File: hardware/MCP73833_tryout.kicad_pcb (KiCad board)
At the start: 2 copper layers, 55 x 30 mm, 14 parts, among them J1 LOAD, J2 BAT, U1 MCP73833, U2 USB_Micro

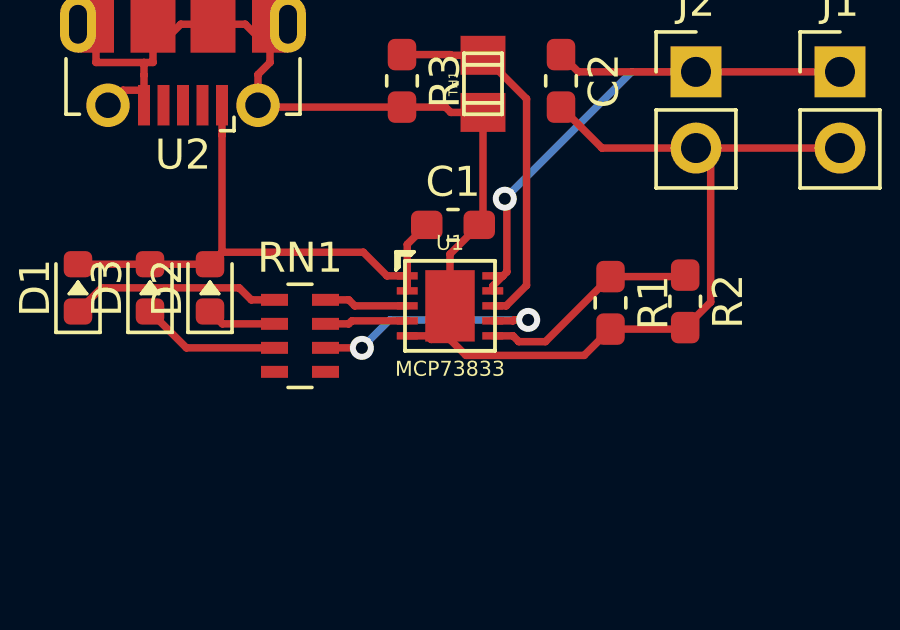
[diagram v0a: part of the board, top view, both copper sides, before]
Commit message: update for MCP73833 DFN,
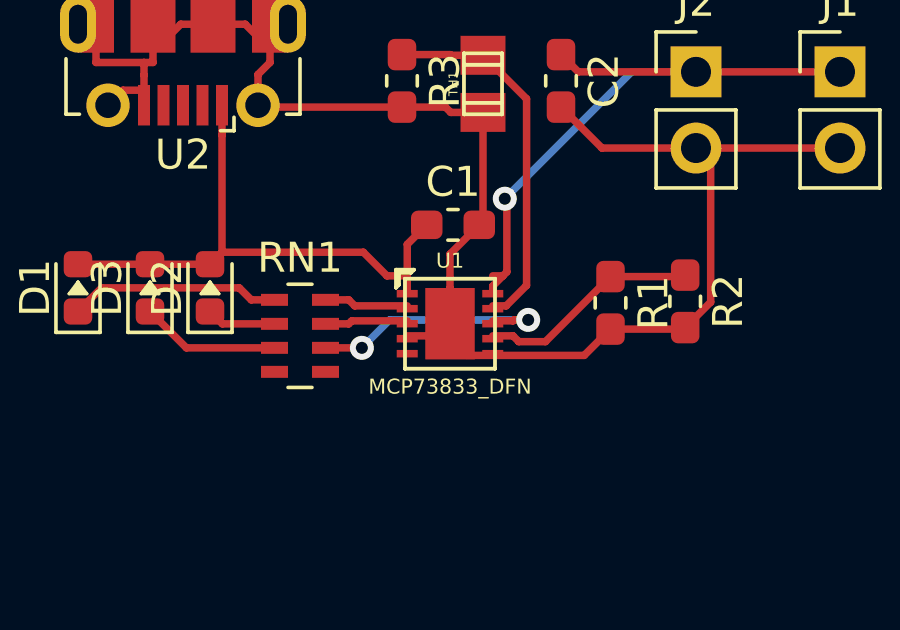
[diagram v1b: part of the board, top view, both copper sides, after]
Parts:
- U1: value MCP73833 -> MCP73833_DFN; footprint footprint-lib:MCP73833 -> footprint-lib:MCP73833_DFN
- moved U1 0.59 mm to (37.0, 31.6)
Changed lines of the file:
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@@
     (add_net "Net-(R1-Pad1)")
     (add_net "Net-(R3-Pad1)")
+    (add_net "Net-(RN1-Pad4)")
+    (add_net "Net-(RN1-Pad5)")
     (add_net "Net-(RN1-Pad6)")
     (add_net "Net-(RN1-Pad7)")
     (add_net "Net-(RN1-Pad8)")
+    (add_net "Net-(U2-Pad2)")
+    (add_net "Net-(U2-Pad3)")
+    (add_net "Net-(U2-Pad4)")
+  )
+  (module footprint-lib:MCP73833_DFN (layer F.Cu)
+    (at 37 31.595)
+    (descr "Plastic DFN, 10 pins, 3x3, Linear Technology")
+    (tags MCP73833_DFN)
+    (fp_text reference U1 (at 0 -2.1) (layer F.SilkS)
+      (effects (font (size 0.5 0.5) (thickness 0.1)))
+    )
+    (fp_text value MCP73833_DFN (at 0 2.1) (layer F.SilkS)
+      (effects (font (size 0.5 0.5) (thickness 0.1)))
+    )
+    (fp_line (start -1.7 -1.3) (end -1.8 -1.2) (layer F.SilkS) (width 0.127))
+    (fp_line (start -1.8 -1.2) (end -1.8 -1.8) (layer F.SilkS) (width 0.127))
+    (fp_line (start -1.8 -1.8) (end -1.2 -1.8) (layer F.SilkS) (width 0.127))
+    (fp_line (start -1.2 -1.8) (end -1.3 -1.7) (layer F.SilkS) (width 0.127))
+    (fp_line (start -1.3 -1.7) (end -1.7 -1.7) (layer F.SilkS) (width 0.127))
+    (fp_line (start -1.7 -1.7) (end -1.7 -1.3) (layer F.SilkS) (width 0.127))
+    (fp_line (start -1.5 -1.5) (end -1.5 1.5) (layer F.SilkS) (width 0.127))
+    (fp_line (start -1.5 1.5) (end 1.5 1.5) (layer F.SilkS) (width 0.127))
+    (fp_line (start 1.5 1.5) (end 1.5 -1.5) (layer F.SilkS) (width 0.127))
+    (fp_line (start 1.5 -1.5) (end -1.5 -1.5) (layer F.SilkS) (width 0.127))
+    (pad 1 smd rect (at -1.425 -1) (size 0.7 0.25) (layers F.Cu F.Paste F.Mask)
+      (net 2 +5V) (solder_mask_margin 0.07))
+    (pad 2 smd rect (at -1.425 -0.5) (size 0.7 0.25) (layers F.Cu F.Paste F.Mask)
+      (net 2 +5V) (solder_mask_margin 0.07))
+    (pad 3 smd rect (at -1.425 0) (size 0.7 0.25) (layers F.Cu F.Paste F.Mask)
+      (net 11 "Net-(RN1-Pad8)") (solder_mask_margin 0.07))
+    (pad 4 smd rect (at -1.425 0.5) (size 0.7 0.25) (layers F.Cu F.Paste F.Mask)
+      (net 10 "Net-(RN1-Pad7)") (solder_mask_margin 0.07))
+    (pad 5 smd rect (at -1.425 1) (size 0.7 0.25) (layers F.Cu F.Paste F.Mask)
+      (net 1 GND) (solder_mask_margin 0.07))
+    (pad 6 smd rect (at 1.425 1) (size 0.7 0.25) (layers F.Cu F.Paste F.Mask)
+      (net 7 "Net-(R1-Pad1)") (solder_mask_margin 0.07))
+    (pad 7 smd rect (at 1.425 0.5) (size 0.7 0.25) (layers F.Cu F.Paste F.Mask)
+      (net 9 "Net-(RN1-Pad6)") (solder_mask_margin 0.07))
+    (pad 8 smd rect (at 1.425 0) (size 0.7 0.25) (layers F.Cu F.Paste F.Mask)
+      (net 8 "Net-(R3-Pad1)") (solder_mask_margin 0.07))
+    (pad 9 smd rect (at 1.425 -0.5) (size 0.7 0.25) (layers F.Cu F.Paste F.Mask)
+      (net 3 "Net-(C2-Pad1)") (solder_mask_margin 0.07))
+    (pad 10 smd rect (at 1.425 -1) (size 0.7 0.25) (layers F.Cu F.Paste F.Mask)
+      (net 3 "Net-(C2-Pad1)") (solder_mask_margin 0.07))
+    (pad 11 smd rect (at 0 -0.595) (size 1.65 1.19) (layers F.Cu F.Paste F.Mask)
+      (net 1 GND) (solder_mask_margin 0.07) (solder_paste_margin -0.1))
+    (pad 11 smd rect (at 0 0.595) (size 1.65 1.19) (layers F.Cu F.Paste F.Mask)
+      (net 1 GND) (solder_mask_margin 0.07) (solder_paste_margin -0.1))
+    (model ${HOME}/_workspace/kicad/kicad_library/smisioto-footprints/modules/packages3d/walter/smd_qfn/dfn10_3x3.wrl
+      (at (xyz 0 0 0))
+      (scale (xyz 1 1 1))
+      (rotate (xyz 0 0 0))
+    )
   )
   (module footprint-lib:USB_Micro-B_Molex-105017-0001 (layer F.Cu)
@@
       (rotate (xyz 0 0 0))
     )
-  )
-  (module footprint-lib:MCP73833 (layer F.Cu)
-    (at 37 31)
-    (descr "Plastic DFN, 10 pins, 3x3, Linear Technology")
-    (tags MCP73833)
-    (fp_text reference U1 (at 0 -2.1) (layer F.SilkS)
-      (effects (font (size 0.5 0.5) (thickness 0.1)))
-    )
-    (fp_text value MCP73833 (at 0 2.1) (layer F.SilkS)
-      (effects (font (size 0.5 0.5) (thickness 0.1)))
-    )
-    (fp_line (start -1.7 -1.3) (end -1.8 -1.2) (layer F.SilkS) (width 0.127))
-    (fp_line (start -1.8 -1.2) (end -1.8 -1.8) (layer F.SilkS) (width 0.127))
-    (fp_line (start -1.8 -1.8) (end -1.2 -1.8) (layer F.SilkS) (width 0.127))
-    (fp_line (start -1.2 -1.8) (end -1.3 -1.7) (layer F.SilkS) (width 0.127))
-    (fp_line (start -1.3 -1.7) (end -1.7 -1.7) (layer F.SilkS) (width 0.127))
-    (fp_line (start -1.7 -1.7) (end -1.7 -1.3) (layer F.SilkS) (width 0.127))
-    (fp_line (start -1.5 -1.5) (end -1.5 1.5) (layer F.SilkS) (width 0.127))
-    (fp_line (start -1.5 1.5) (end 1.5 1.5) (layer F.SilkS) (width 0.127))
-    (fp_line (start 1.5 1.5) (end 1.5 -1.5) (layer F.SilkS) (width 0.127))
-    (fp_line (start 1.5 -1.5) (end -1.5 -1.5) (layer F.SilkS) (width 0.127))
-    (pad 1 smd rect (at -1.425 -1) (size 0.7 0.25) (layers F.Cu F.Paste F.Mask)
-      (net 2 +5V) (solder_mask_margin 0.07))
-    (pad 2 smd rect (at -1.425 -0.5) (size 0.7 0.25) (layers F.Cu F.Paste F.Mask)
-      (net 2 +5V) (solder_mask_margin 0.07))
-    (pad 3 smd rect (at -1.425 0) (size 0.7 0.25) (layers F.Cu F.Paste F.Mask)
-      (net 11 "Net-(RN1-Pad8)") (solder_mask_margin 0.07))
-    (pad 4 smd rect (at -1.425 0.5) (size 0.7 0.25) (layers F.Cu F.Paste F.Mask)
-      (net 10 "Net-(RN1-Pad7)") (solder_mask_margin 0.07))
-    (pad 5 smd rect (at -1.425 1) (size 0.7 0.25) (layers F.Cu F.Paste F.Mask)
-      (net 1 GND) (solder_mask_margin 0.07))
-    (pad 6 smd rect (at 1.425 1) (size 0.7 0.25) (layers F.Cu F.Paste F.Mask)
-      (net 7 "Net-(R1-Pad1)") (solder_mask_margin 0.07))
-    (pad 7 smd rect (at 1.425 0.5) (size 0.7 0.25) (layers F.Cu F.Paste F.Mask)
-      (net 9 "Net-(RN1-Pad6)") (solder_mask_margin 0.07))
-    (pad 8 smd rect (at 1.425 0) (size 0.7 0.25) (layers F.Cu F.Paste F.Mask)
-      (net 8 "Net-(R3-Pad1)") (solder_mask_margin 0.07))
-    (pad 9 smd rect (at 1.425 -0.5) (size 0.7 0.25) (layers F.Cu F.Paste F.Mask)
-      (net 3 "Net-(C2-Pad1)") (solder_mask_margin 0.07))
-    (pad 10 smd rect (at 1.425 -1) (size 0.7 0.25) (layers F.Cu F.Paste F.Mask)
-      (net 3 "Net-(C2-Pad1)") (solder_mask_margin 0.07))
-    (pad 11 smd rect (at 0 -0.595) (size 1.65 1.19) (layers F.Cu F.Paste F.Mask)
-      (net 1 GND) (solder_mask_margin 0.07) (solder_paste_margin -0.1))
-    (pad 11 smd rect (at 0 0.595) (size 1.65 1.19) (layers F.Cu F.Paste F.Mask)
-      (net 1 GND) (solder_mask_margin 0.07) (solder_paste_margin -0.1))
-    (model ${HOME}/_workspace/kicad/kicad_library/smisioto-footprints/modules/packages3d/walter/smd_qfn/dfn10_3x3.wrl
-      (at (xyz 0 0 0))
-      (scale (xyz 1 1 1))
-      (rotate (xyz 0 0 0))
-    )
